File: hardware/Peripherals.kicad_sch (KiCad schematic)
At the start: 1 part, among them J6 USB_C_Receptacle_USB2.0_16P

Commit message: added more stuff wip
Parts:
- removed J6: USB_C_Receptacle_USB2.0_16P, UTSVT_ICs:USB_C_Receptacle_GCT_USB4105-xx-A_16P_TopMnt_Horizontal, symbol utsvt_connectors:USB_C_Receptacle_USB2.0_16P
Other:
- added sheet ESP32_LDO (ESP32_LDO.kicad_sch)
- added sheet ESP32_Power_Mux (ESP32_Power_Mux.kicad_sch)
- sheet ESP32 ports: added +3.3V_MUX_OUT, +5V_LDO_IN, ESP_GPIO1, ESP_GPIO2, ESP_GPIO3, ESP_GPIO4, ESP_RESET, ESP_UART_RX, ESP_UART_TX, GND; removed none

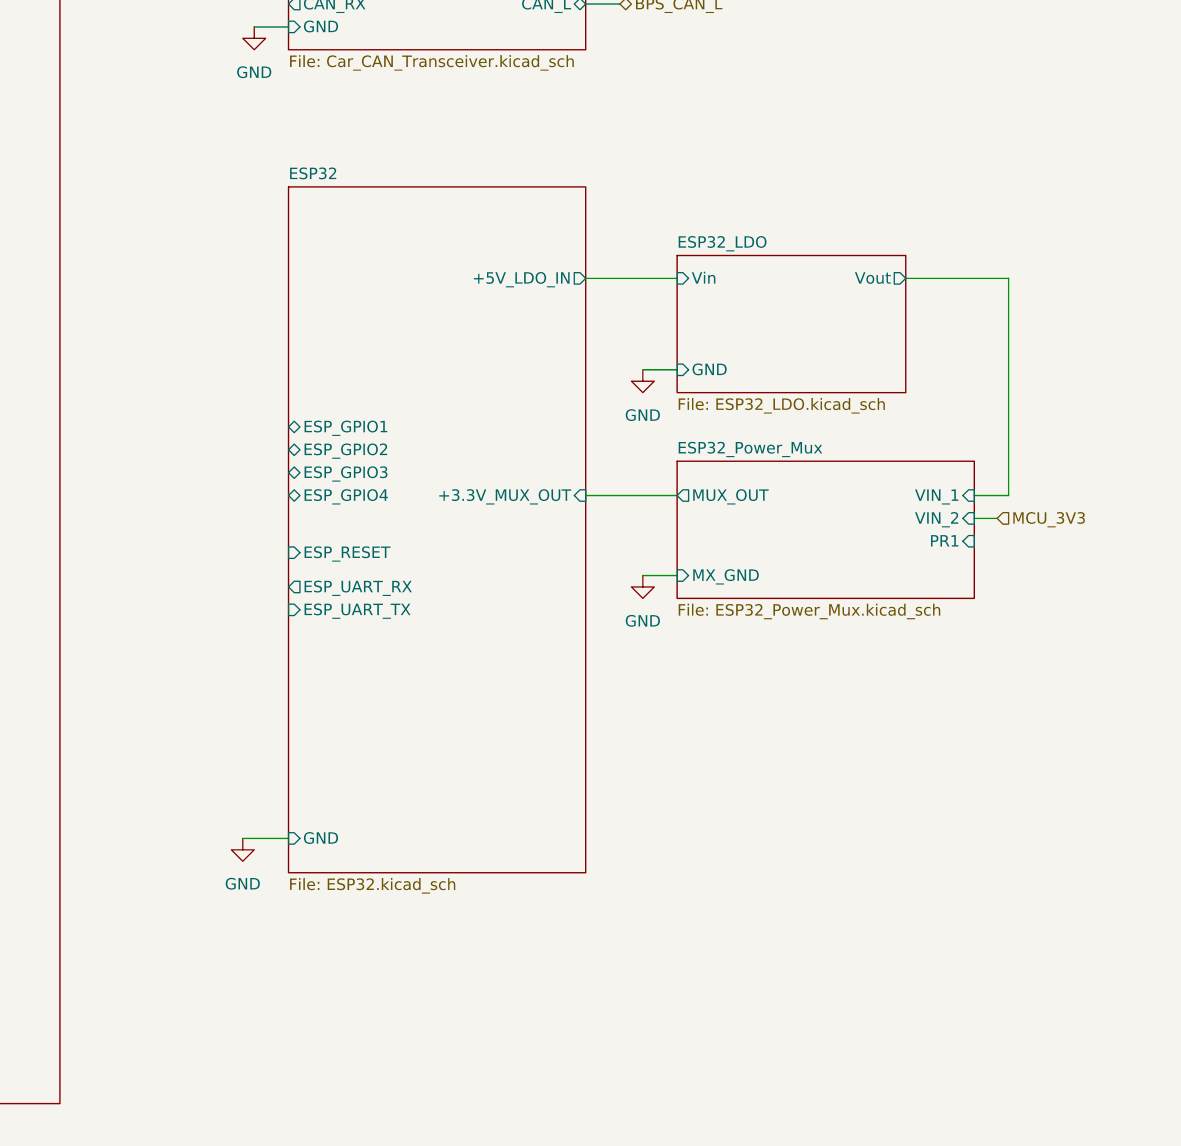
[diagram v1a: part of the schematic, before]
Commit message: some changes - switched to contactor design block - switched to power protection design block - added SD card - added fan I2C pullup - added resistors for ESP32 power mux - shield tied to gnd with 0 ohm - added USB-PD and boost design blocks
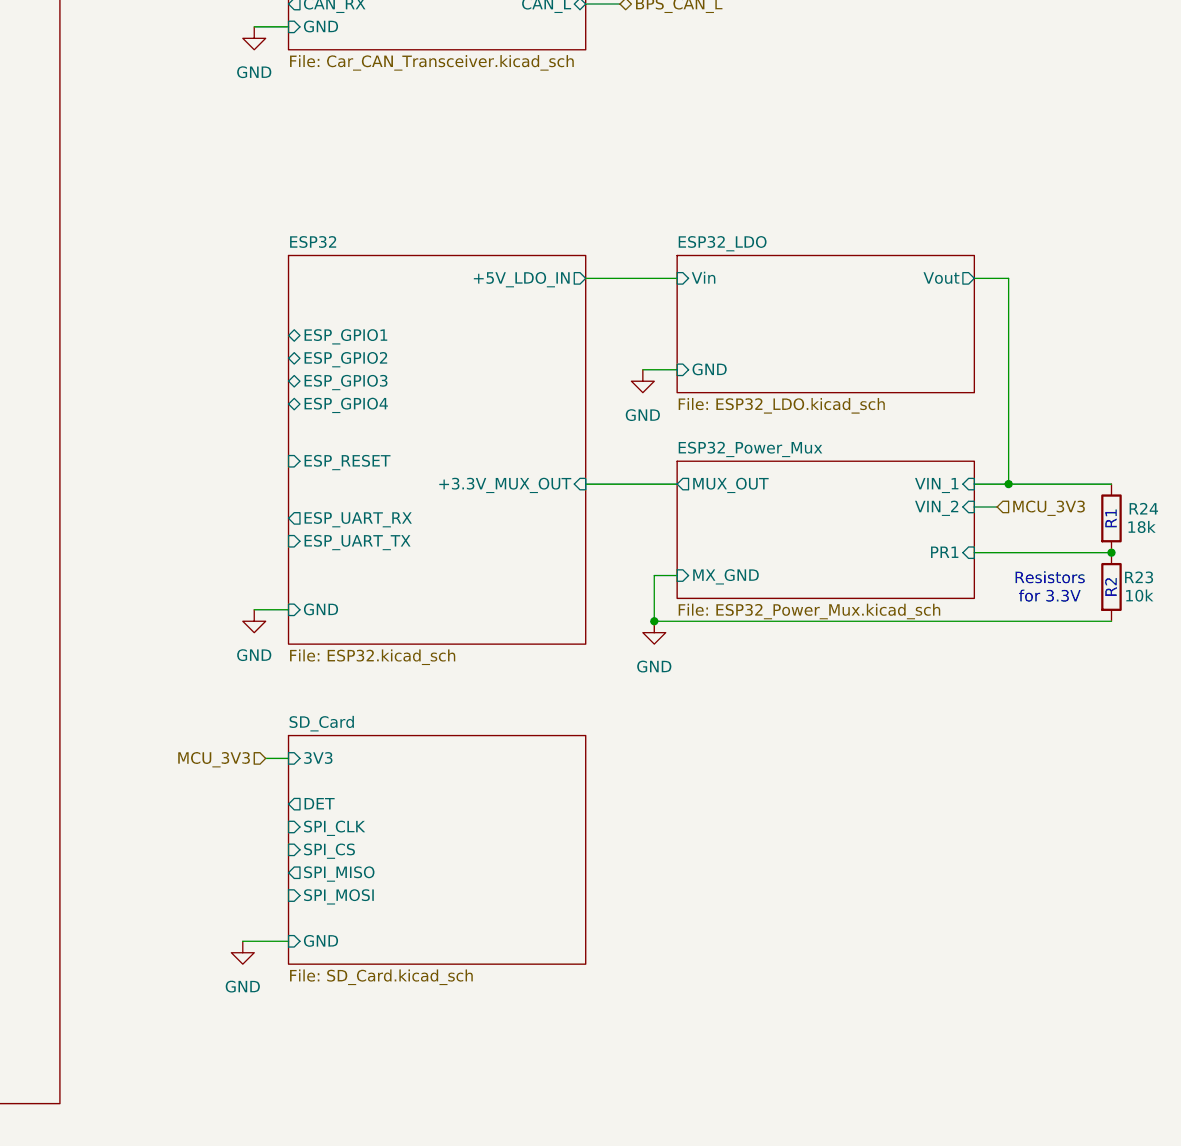
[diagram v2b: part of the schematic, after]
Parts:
- added R23: 10k, Resistor_SMD:R_0603_1608Metric_Pad0.98x0.95mm_HandSolder, symbol Device:R
- added R24: 18k, Resistor_SMD:R_0603_1608Metric_Pad0.98x0.95mm_HandSolder, symbol Device:R
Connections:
- net ESP32_LDO/Vout: now also R24.1
- net ESP32_Power_Mux/PR1: now also R23.1, R24.2
- net GND: now also R23.2
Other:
- added sheet SD_Card (SD_Card.kicad_sch)
- note added: "R1"
- note added: "R2"
- note added: "Resistors for 3.3V"

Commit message: power updates
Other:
- note added: "3.3V Mux"
- note removed: "Resistors for 3.3V"
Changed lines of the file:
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@@
 		)
 	)
-	(text "Resistors\nfor 3.3V"
+	(text "3.3V Mux"
 		(exclude_from_sim no)
 		(at 211.582 120.904 0)
@@
 	(wire
 		(pts
-			(xy 203.2 86.36) (xy 207.01 86.36)
+			(xy 195.58 86.36) (xy 207.01 86.36)
 		)
 		(stroke
@@
 	(sheet
 		(at 127 137.16)
-		(size 33.02 25.4)
+		(size 22.86 25.4)
 		(exclude_from_sim no)
 		(in_bom yes)
@@
 	(sheet
 		(at 170.18 83.82)
-		(size 33.02 15.24)
+		(size 25.4 15.24)
 		(exclude_from_sim no)
 		(in_bom yes)
@@
 		)
 		(pin "Vout" output
-			(at 203.2 86.36 0)
-			(effects
-				(font
+			(at 195.58 86.36 0)
+			(effects
+				(font

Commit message: why is everything weird
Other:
- sheet 100PinMCU ports: added 3V3, BOOT, GND, GNDA, PA0, PA1, PA10, PA15, PA2, PA3, PA4, PA5, PA6, PA7, PA8, PA9, PB0, PB1, PB10, PB11, PB12, PB13, PB14, PB15, PB2, PB3, PB4, PB5, PB6, PB7, PB9, PC0, PC1, PC10, PC11, PC12, PC2, PC3, PC4, PC5, PC6, PC7, PC8, PC9, PD0, PD1, PD10, PD11, PD12, PD13, PD14, PD15, PD2, PD3, PD4, PD5, PD6, PD7, PD8, PD9, PE0, PE1, PE11, PE12, PE13, PE14, PE15, PE2, PE3, PE4, PE5, PE6, PE7, PE8, PE9, PF10, PF2, PF9, PG10-NRST, USB_DM, USB_DP, VDDA; removed none
- moved on the sheet: R23, R24

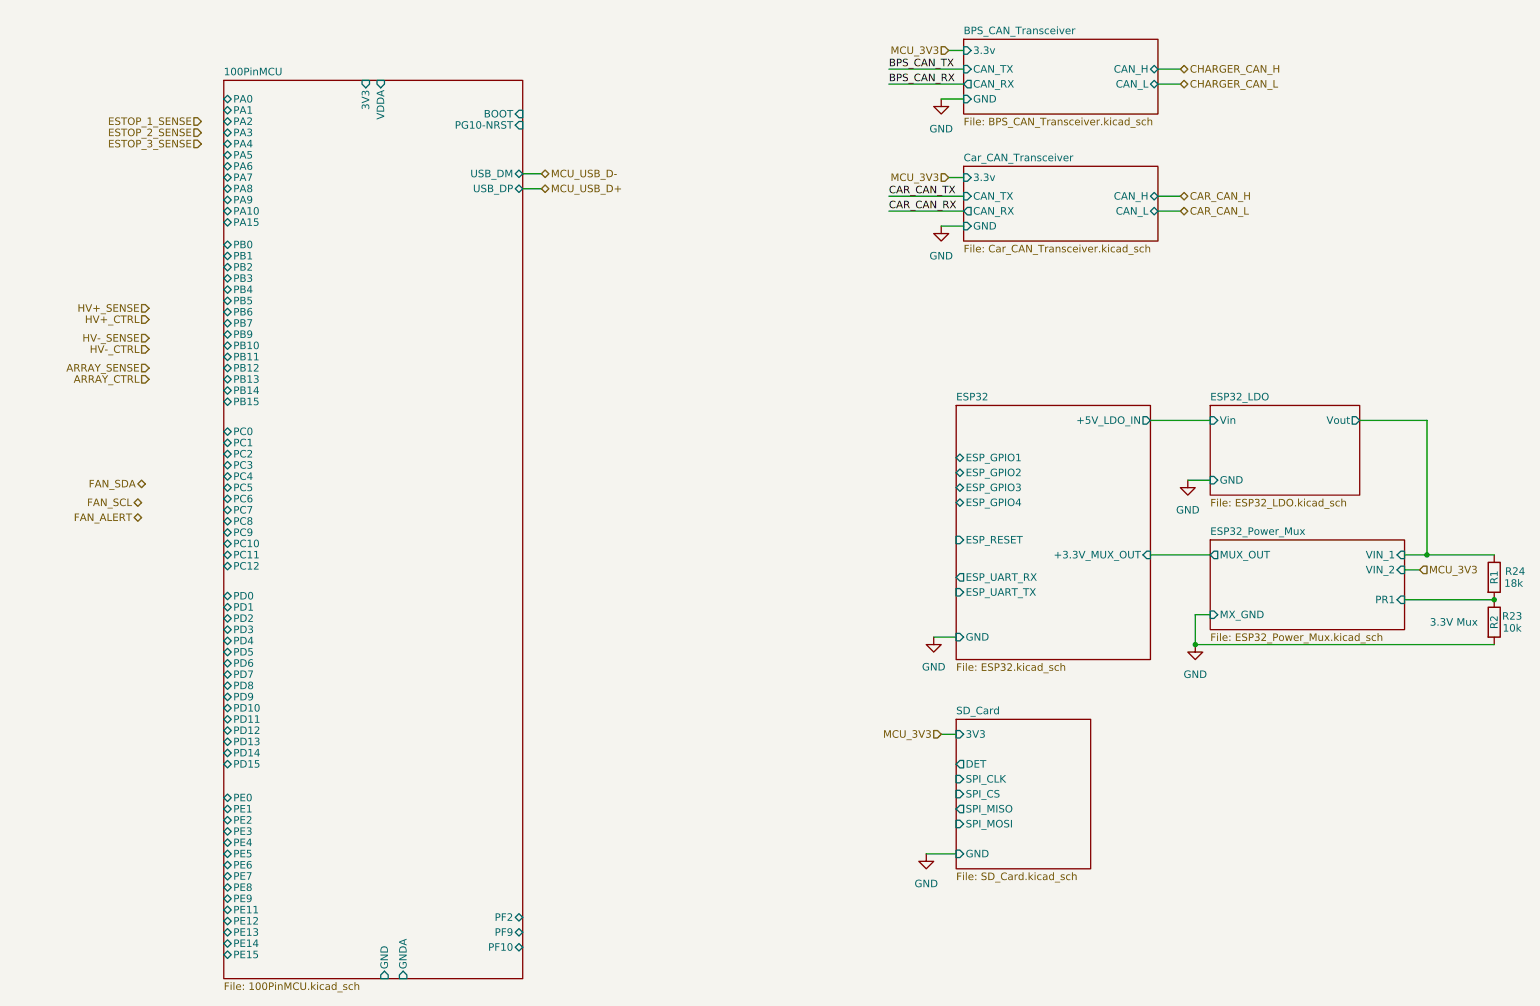
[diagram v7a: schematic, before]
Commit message: finished schematic except for 12v buck boost
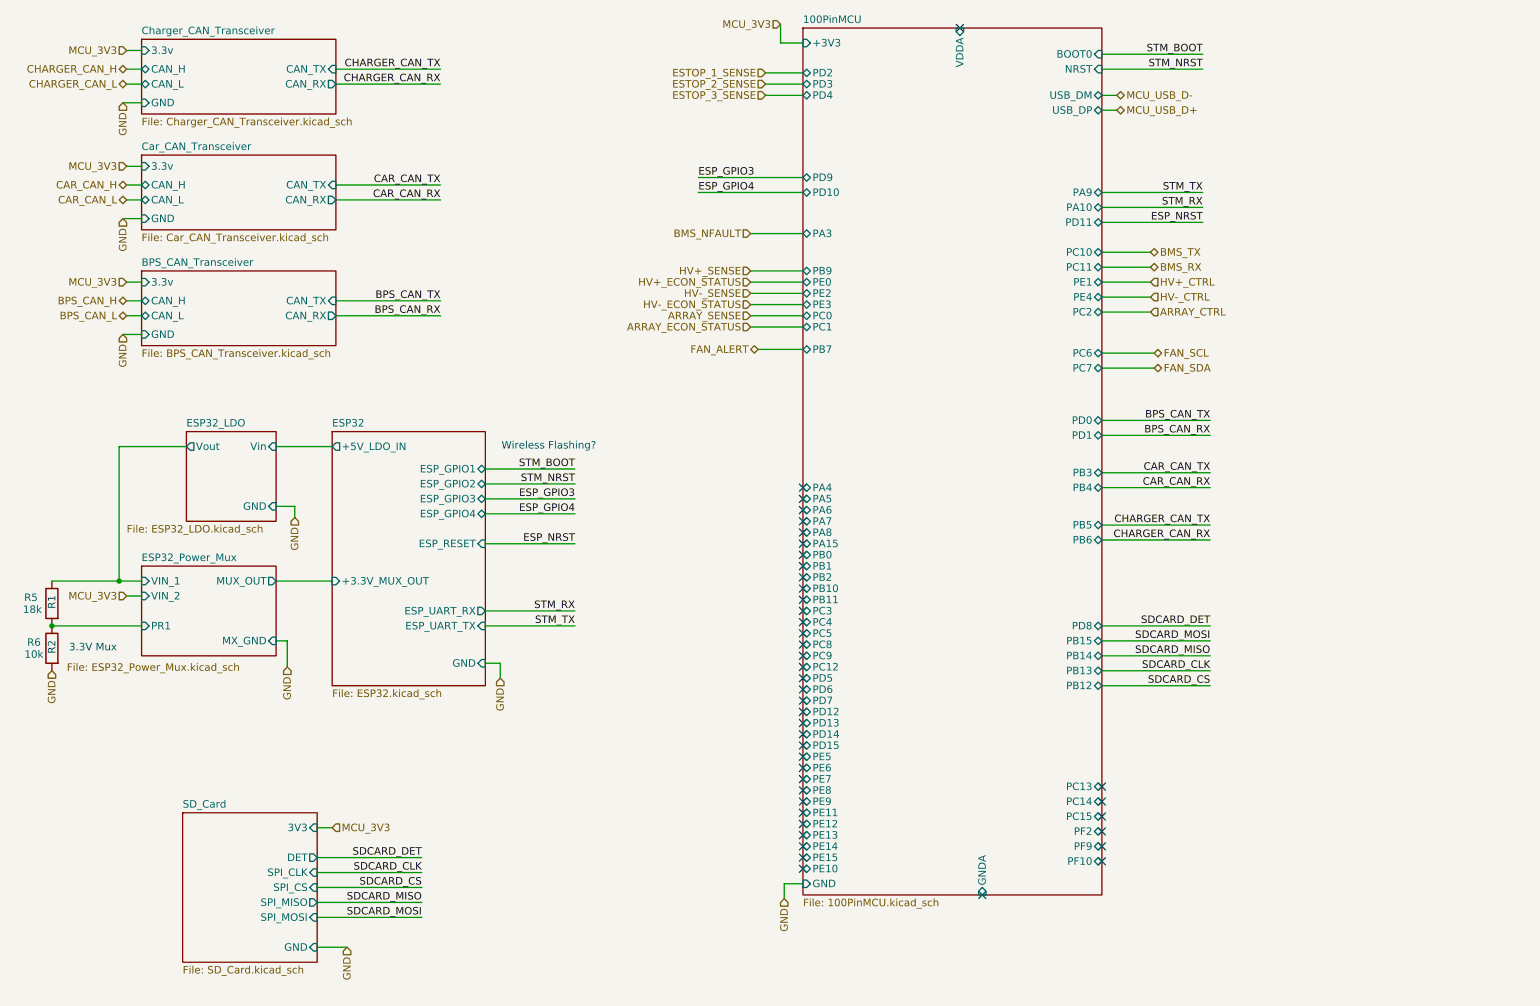
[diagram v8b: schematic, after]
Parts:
- renumbered R24 to R5, R23 to R6
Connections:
- no-connect marks 0 -> 43
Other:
- added sheet Charger_CAN_Transceiver (Charger_CAN_Transceiver.kicad_sch)
- sheet 100PinMCU ports: added +3V3, BOOT0, NRST, PC13, PC14, PC15, PE10; removed 3V3, BOOT, PA0, PA1, PA2, PG10-NRST
- note added: "Wireless Flashing?"
- moved on the sheet: R5, R6
